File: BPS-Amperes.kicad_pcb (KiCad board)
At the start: 2 copper layers, 40 x 50 mm, 39 parts, among them J1 Conn_02x10_Odd_Even, J2 ShuntConn, J3 PassthroughConn, J4 TestConn, U1 INA186A3IDDFT, U2 OPA2196, U3 LTC2315, U4 REF1930AIDDCT

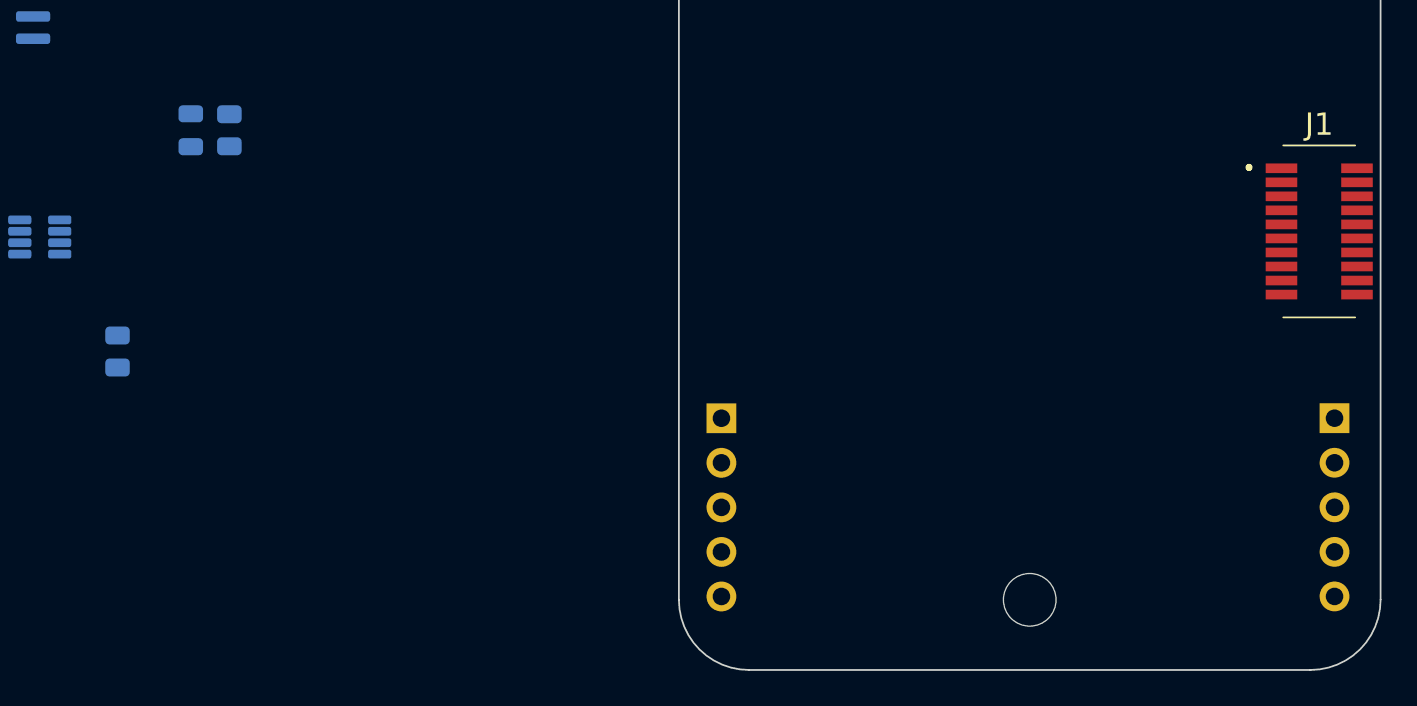
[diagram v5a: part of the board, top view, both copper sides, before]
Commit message: fix shunt conn positions
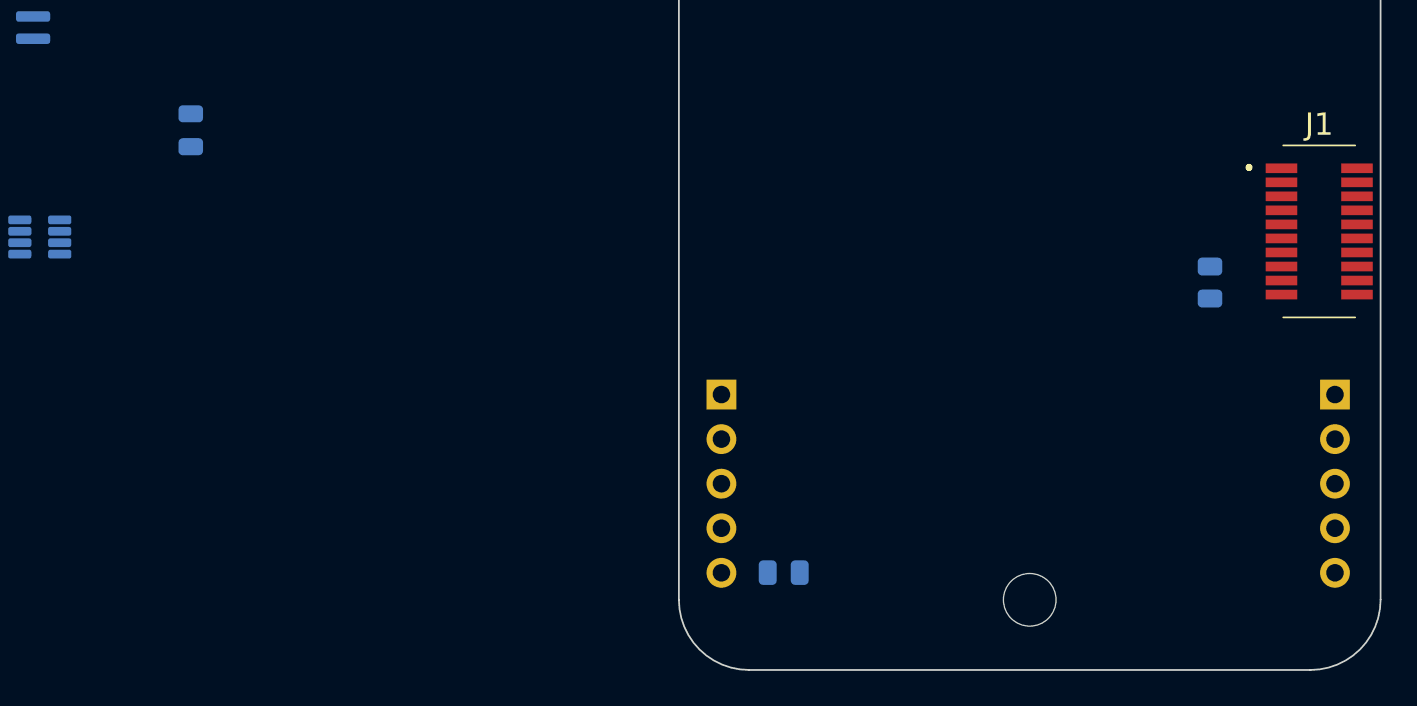
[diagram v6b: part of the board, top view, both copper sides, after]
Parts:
- moved R7 62.4 mm to (160.3, 93.9)
- moved R6 40.4 mm to (136.0, 110.5), turned to 180 degrees
- moved J2 1.35 mm to (132.4, 100.3)
- moved J3 1.35 mm to (167.4, 100.3)
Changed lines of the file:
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@@
   )
   (footprint "Connector_PinSocket_2.54mm:PinSocket_1x05_P2.54mm_Vertical" (layer "B.Cu")
-    (at 132.425 101.65 180)
+    (at 132.425 100.3 180)
     (descr "Through hole straight socket strip, 1x05, 2.54mm pitch, single row (from Kicad 4.0.7), script generated")
     (tags "Through hole socket strip THT 1x05 2.54mm single row")
@@
   )
   (footprint "Resistor_SMD:R_0805_2012Metric" (layer "B.Cu")
-    (at 97.9994 97.845 -90)
+    (at 160.275 93.9125 -90)
     (descr "Resistor SMD 0805 (2012 Metric), square (rectangular) end terminal, IPC_7351 nominal, (Body size source: IPC-SM-782 page 72, https://www.pcb-3d.com/wordpress/wp-content/uploads/ipc-sm-782a_amendment_1_and_2.pdf), generated with kicad-footprint-generator")
     (tags "resistor")
@@
   )
   (footprint "Resistor_SMD:R_0805_2012Metric" (layer "B.Cu")
-    (at 104.3744 85.2325 90)
+    (at 135.975 110.45 180)
     (descr "Resistor SMD 0805 (2012 Metric), square (rectangular) end terminal, IPC_7351 nominal, (Body size source: IPC-SM-782 page 72, https://www.pcb-3d.com/wordpress/wp-content/uploads/ipc-sm-782a_amendment_1_and_2.pdf), generated with kicad-footprint-generator")
     (tags "resistor")
@@
     (property "ki_keywords" "r resistor")
     (attr smd)
-    (fp_text reference "R6" (at 0 1.65 90) (layer "B.SilkS")
+    (fp_text reference "R6" (at 0 1.65) (layer "B.SilkS")
         (effects (font (size 1 1) (thickness 0.15)) (justify mirror))
     )
-    (fp_text value "1.5k" (at 0 -1.65 90) (layer "B.Fab")
+    (fp_text value "1.5k" (at 0 -1.65) (layer "B.Fab")
         (effects (font (size 1 1) (thickness 0.15)) (justify mirror))
     )
-    (fp_text user "${REFERENCE}" (at 0 0 90) (layer "B.Fab")
+    (fp_text user "${REFERENCE}" (at 0 0) (layer "B.Fab")
         (effects (font (size 0.5 0.5) (thickness 0.08)) (justify mirror))
     )
@@
     (fp_line (start 1 0.625) (end 1 -0.625)
       (stroke (width 0.1) (type solid)) (layer "B.Fab"))
-    (pad "1" smd roundrect (at -0.9125 0 90) (size 1.025 1.4) (layers "B.Cu" "B.Paste" "B.Mask") (roundrect_rratio 0.243902)
+    (pad "1" smd roundrect (at -0.9125 0 180) (size 1.025 1.4) (layers "B.Cu" "B.Paste" "B.Mask") (roundrect_rratio 0.243902)
       (net 2 "+3.3V") (pintype "passive"))
-    (pad "2" smd roundrect (at 0.9125 0 90) (size 1.025 1.4) (layers "B.Cu" "B.Paste" "B.Mask") (roundrect_rratio 0.243902)
+    (pad "2" smd roundrect (at 0.9125 0 180) (size 1.025 1.4) (layers "B.Cu" "B.Paste" "B.Mask") (roundrect_rratio 0.243902)
       (net 27 "Net-(D2-A)") (pintype "passive"))
     (model "${KICAD6_3DMODEL_DIR}/Resistor_SMD.3dshapes/R_0805_2012Metric.wrl"
@@
   )
   (footprint "Connector_PinSocket_2.54mm:PinSocket_1x05_P2.54mm_Vertical" (layer "B.Cu")
-    (at 167.3748 101.6474 180)
+    (at 167.4 100.3 180)
     (descr "Through hole straight socket strip, 1x05, 2.54mm pitch, single row (from Kicad 4.0.7), script generated")
     (tags "Through hole socket strip THT 1x05 2.54mm single row")
@@
   )
   (dimension (type orthogonal) (layer "Dwgs.User")
-    (pts (xy 132.425 101.65) (xy 167.4002 101.6982))
+    (pts (xy 132.425 100.3) (xy 167.4002 100.3482))
     (height -13.0328)
     (orientation 0)
-    (gr_text "34.9752 mm" (at 149.9126 87.4672) (layer "Dwgs.User")
+    (gr_text "34.9752 mm" (at 149.9126 86.1172) (layer "Dwgs.User")
       (effects (font (size 1 1) (thickness 0.15)))
     )

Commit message: Fix possible issue and revert
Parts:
- moved C13 96.0 mm to (167.5, 83.8), turned to 180 degrees
- moved FB2 88.3 mm to (160.4, 83.7), turned to 180 degrees
- moved FB1 88.2 mm to (161.9, 79.5), turned to 180 degrees
- moved C12 86.9 mm to (153.0, 85.2)
- moved C11 86.3 mm to (155.9, 85.2)
- moved U4 76.8 mm to (152.5, 89.3)
- moved C10 69.1 mm to (148.4, 78.5), turned to -90 degrees
- moved D2 67.6 mm to (168.4, 71.9), turned to -90 degrees
- moved R6 44.1 mm to (168.6, 80.8), turned to 90 degrees
- moved TP3 41.5 mm to (134.9, 79.8)
- moved TP2 36.1 mm to (135.0, 75.5)
- moved C8 28.2 mm to (97.7, 89.7), turned to 180 degrees
- moved C2 8.64 mm to (74.8, 72.5)
- moved R2 2.06 mm to (72.5, 84.4)
- moved R7 1.62 mm to (159.8, 95.5)
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
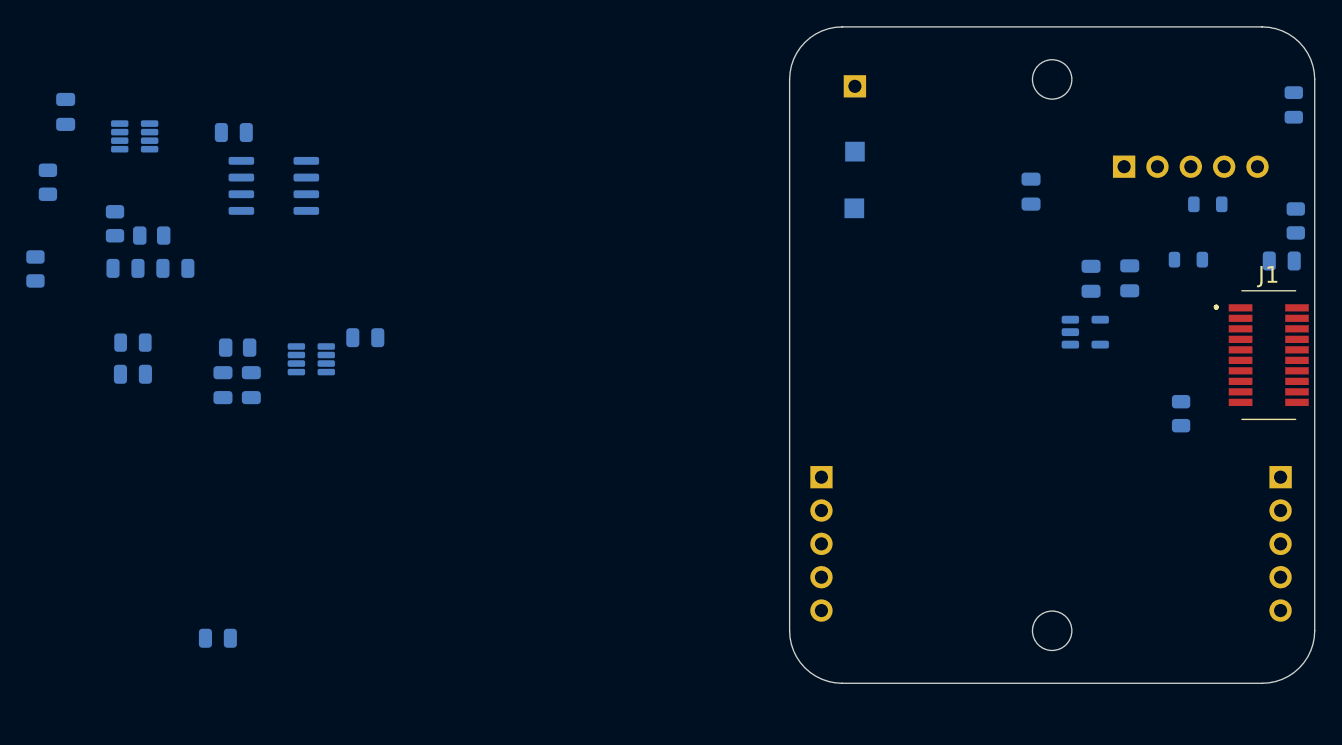
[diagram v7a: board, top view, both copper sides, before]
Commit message: Changed testpoints and arranged power components
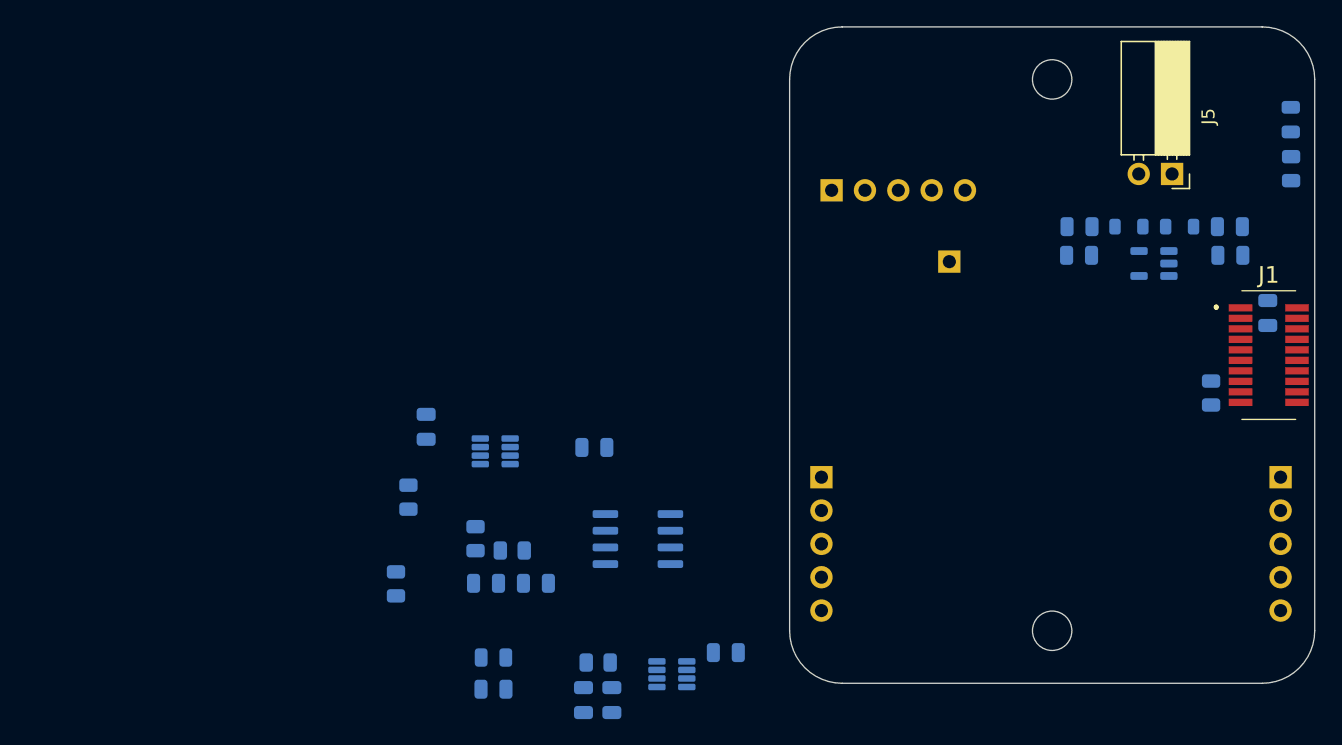
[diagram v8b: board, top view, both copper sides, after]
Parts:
- removed TP2: +1V5_TP, TestPoint:TestPoint_Pad_1.5x1.5mm
- removed TP3: +3V0_TP, TestPoint:TestPoint_Pad_1.5x1.5mm
- added J5: Conn_01x02, Connector_PinSocket_2.54mm:PinSocket_1x02_P2.54mm_Horizontal, F.Cu at (159.1, 77.2)
- TP1: footprint Connector_PinSocket_2.54mm:PinSocket_1x01_P2.54mm_Vertical -> Connector_PinSocket_2.54mm:PinSocket_1x01_P2.54mm_Horizontal
- moved C9 82.5 mm to (163.6, 83.4), turned to 0 degrees
- moved U2 38.6 mm to (118.4, 105.0)
- moved C7 36.5 mm to (116.5, 117.3)
- moved R3 36.5 mm to (106.1, 105.0)
- moved C1 36.5 mm to (115.1, 98.0)
- moved C2 36.5 mm to (102.3, 96.5)
- moved C3 36.5 mm to (106.9, 108.4)
- moved C4 36.5 mm to (110.7, 108.4)
- moved C5 36.5 mm to (114.3, 117.3)
- moved C6 36.5 mm to (107.4, 116.5)
- moved C8 36.5 mm to (125.1, 113.7)
- moved D1 36.5 mm to (107.4, 114.0)
- moved R1 36.5 mm to (101.0, 101.8)
- moved R2 36.5 mm to (100.0, 108.4)
- moved R4 36.5 mm to (108.9, 105.9)
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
